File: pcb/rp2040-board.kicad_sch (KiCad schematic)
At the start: 57 parts, among them J1 DMX, J2 GPIO, J3 ELRS, J4 OLED, J5 SWD, J6 USB_C_Receptacle_USB2.0_16P, SW1 TS-1187A-B-A-B, SW2 RotaryEncoder_Switch, SW3 TS-1187A-B-A-B, U1 W25Q128JVS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

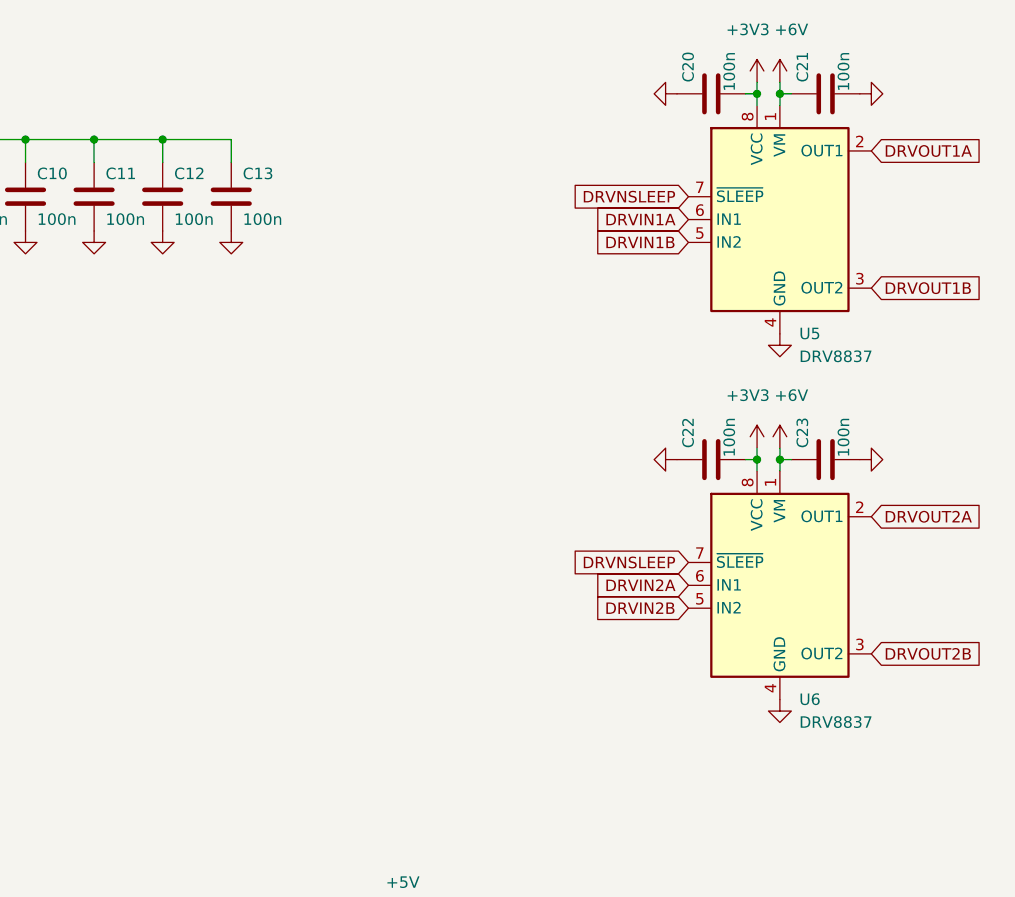
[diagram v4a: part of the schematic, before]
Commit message: add motor drivers and split the schematic
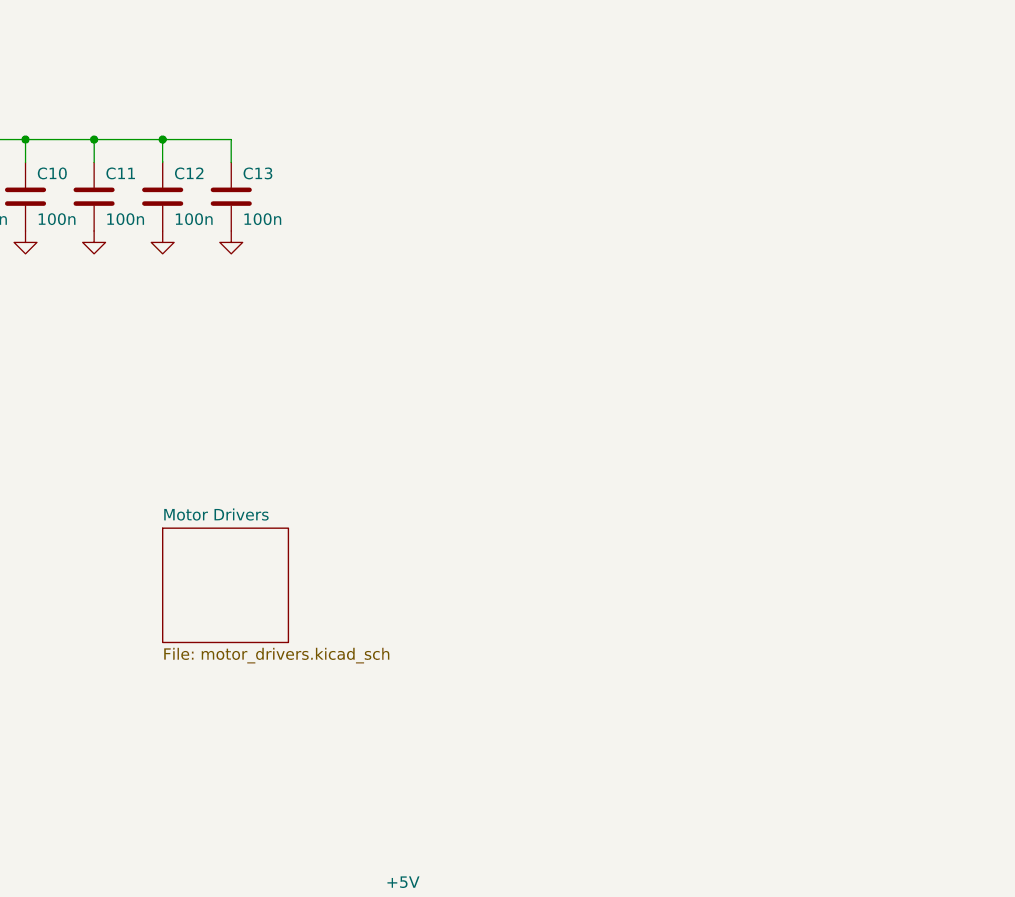
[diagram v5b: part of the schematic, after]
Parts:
- removed C20, C21, C22, C23: 100n, Capacitor_SMD:C_0402_1005Metric, symbol Device:C
- removed U5, U6: DRV8837, Package_SON:WSON-8-1EP_2x2mm_P0.5mm_EP0.9x1.6mm, symbol Driver_Motor:DRV8837
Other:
- added sheet Motor Drivers (motor_drivers.kicad_sch)

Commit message: WIP on the power section of the new board
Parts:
- removed C14: 100n, Capacitor_SMD:C_0402_1005Metric, symbol Device:C
- removed C15: 1u, Capacitor_SMD:C_0402_1005Metric, symbol Device:C
- removed C18, C19: 22u, Capacitor_SMD:C_0805_2012Metric, symbol Device:C
- removed D1, D2, D5: SS34, Diode_SMD:D_SMA, symbol Device:D_Schottky
- removed J1: DMX, Connector_Audio:Jack_XLR_Neutrik_NC3FAAH_Horizontal, symbol Connector_Audio:XLR3
- removed J6: USB_C_Receptacle_USB2.0_16P, Connector_USB:USB_C_Receptacle_G-Switch_GT-USB-7010ASV, symbol Connector:USB_C_Receptacle_USB2.0_16P
- removed R11: 0, Resistor_SMD:R_0603_1608Metric, symbol Device:R
- removed R12: 47, Resistor_SMD:R_0603_1608Metric, symbol Device:R
- removed R13: 120, Resistor_SMD:R_1206_3216Metric, symbol Device:R
- removed R3, R6: 1R, Resistor_SMD:R_0603_1608Metric, symbol Device:R
- removed U2: SP485EEN-L/TR, Package_SO:SOIC-8_3.9x4.9mm_P1.27mm, symbol Interface_UART:MAX485E
- removed U4: AMS1117-3.3, Package_TO_SOT_SMD:SOT-223, symbol Regulator_Linear:XC6206PxxxMR
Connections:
- no-connect marks 5 -> 1
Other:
- added sheet Power (power.kicad_sch)

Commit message: WIP on the motor driver board
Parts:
- removed C1, C10, C11, C12, C13, C3, C4, C7, C8, C9: 100n, Capacitor_SMD:C_0402_1005Metric, symbol Device:C
- removed C16, C17: 22p, Capacitor_SMD:C_0402_1005Metric, symbol Device:C
- removed C2, C5, C6: 1u, Capacitor_SMD:C_0402_1005Metric, symbol Device:C
- removed D3: Yellow, LED_SMD:LED_0603_1608Metric, symbol Device:LED
- removed D4: Red, LED_SMD:LED_0603_1608Metric, symbol Device:LED
- removed J5: SWD, Connector_PinHeader_1.27mm:PinHeader_2x05_P1.27mm_Vertical_SMD, symbol Connector:Conn_ARM_JTAG_SWD_10
- removed R10, R9: 330, Resistor_SMD:R_0402_1005Metric, symbol Device:R
- removed R4, R5: 22, Resistor_SMD:R_0402_1005Metric, symbol Device:R
- removed R7: 1k, Resistor_SMD:R_0402_1005Metric, symbol Device:R
- removed SW1: TS-1187A-B-A-B, Button_Switch_SMD:SW_Push_1P1T_XKB_TS-1187A, symbol Switch:SW_SPST
- removed SW2: RotaryEncoder_Switch, Rotary_Encoder:RotaryEncoder_Bourns_Vertical_PEC12R-3x17F-Sxxxx, symbol Device:RotaryEncoder_Switch
- removed U1: W25Q128JVS, Package_SON:WSON-8-1EP_6x5mm_P1.27mm_EP3.4x4.3mm, symbol Memory_Flash:W25Q32JVZP
- removed U3: RP2040, Package_DFN_QFN:QFN-56-1EP_7x7mm_P0.4mm_EP3.2x3.2mm, symbol MCU_RaspberryPi:RP2040
- removed Y1: 12MHz, Crystal:Crystal_SMD_3225-4Pin_3.2x2.5mm, symbol Device:Crystal_GND24
- added A1: RaspberryPi_Pico, Module:RaspberryPi_Pico_Common_Unspecified, symbol MCU_Module:RaspberryPi_Pico
- added D1, D2, D3, D7: WS2812B-2020, LED_SMD:LED_WS2812B-2020_PLCC4_2.0x2.0mm, symbol LED:WS2812B-2020
- R1: value DNP -> 10k; JLCPCB BOM false -> (none); LCSC Part (none) -> C25744
- R2: value 1k -> 10k; LCSC Part C11702 -> C25744
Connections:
- net OLED_SCK is gone; now on net I2C_SCK: J4.3 (Pin_3)
- net +3V3: now also R2.1, A1.36 (3V3)
- net +5V: now also A1.39 (VSYS), D1.4 (VDD), D2.4 (VDD), D3.4 (VDD), D7.4 (VDD)
- net ELRS_RX: now also A1.27 (GPIO21)
- net ELRS_TX: now also A1.26 (GPIO20)
- net GND: now also A1.13 (GND), A1.18 (GND), A1.23 (GND), A1.28 (GND), A1.3 (GND), A1.33 (AGND), A1.38 (GND), A1.8 (GND), D1.2 (VSS), D2.2 (VSS), D3.2 (VSS), D7.2 (VSS)
- net GPIO10: now also A1.14 (GPIO10)
- net GPIO11: now also A1.15 (GPIO11)
- net GPIO12: now also A1.16 (GPIO12)
- net GPIO13: now also A1.17 (GPIO13)
- net GPIO14: now also A1.19 (GPIO14)
- net GPIO15: now also A1.20 (GPIO15)
- net RE_A: now also A1.22 (GPIO17)
- net RE_B: now also A1.24 (GPIO18)
- net RE_SW: now also A1.25 (GPIO19)
- net RUN: now also A1.30 (RUN)
- net #USB_BOOT renamed I2C_SCK
- net I2C_SCK: now also A1.12 (GPIO9)
- net GPIO00: no longer names the net of J2.5 (Pin_5)
- net GPIO01: no longer names the net of J2.6 (Pin_6)
- net GPIO02: no longer names the net of J2.7 (Pin_7)
- net GPIO03: no longer names the net of J2.8 (Pin_8)
- net GPIO04: no longer names the net of J2.9 (Pin_9)
- net GPIO05: no longer names the net of J2.10 (Pin_10)
- net GPIO06: no longer names the net of J2.11 (Pin_11)
- net GPIO07: no longer names the net of J2.12 (Pin_12)
- net GPIO08: no longer names the net of J2.14 (Pin_14)
- net GPIO09: no longer names the net of J2.15 (Pin_15)
- net OLED_SDA renamed I2C_SDA
- net I2C_SDA: now also R1.2, A1.11 (GPIO8)
- removed net QSPI_SS: R1.2, R2.1
- net VBUS: no longer names the net of J2.1 (Pin_1)
- new net: D2.1 (DOUT), D3.3 (DIN)
- new net: D1.1 (DOUT), D2.3 (DIN)
- new net: D1.3 (DIN), D7.1 (DOUT)
- new net DRVIN1A: A1.1 (GPIO0)
- new net DRVIN1B: A1.2 (GPIO1)
- new net DRVIN2A: A1.4 (GPIO2)
- new net DRVIN2B: A1.5 (GPIO3)
- new net DRVIN3A: A1.6 (GPIO4)
- new net DRVIN3B: A1.7 (GPIO5)
- new net DRVIN4A: A1.9 (GPIO6)
- new net DRVIN4B: A1.10 (GPIO7)
- new net LED_DIN: A1.21 (GPIO16), D7.3 (DIN)
- new net LED_DOUT: D3.1 (DOUT)
- no-connect marks 1 -> 4
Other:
- note removed: "USB Boot"
- moved on the sheet: J2, J3, J4

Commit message: wip on pcb
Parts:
- A1: footprint Module:RaspberryPi_Pico_Common_Unspecified -> Module:RaspberryPi_Pico_Common_SMD
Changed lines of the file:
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@@
 			)
 		)
-		(property "Footprint" "Module:RaspberryPi_Pico_Common_Unspecified"
+		(property "Footprint" "Module:RaspberryPi_Pico_Common_SMD"
 			(at 134.62 142.24 0)
 			(effects
